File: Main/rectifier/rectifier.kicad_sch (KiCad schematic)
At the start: 15 parts, among them J2 Jack-DC, J3 Screw_Terminal_01x02, Q1 BS170, U1 ESP32-C3-WROOM-02, U2 LM2596S-5, U3 HC-SR04, U4 DM-OLED096-636

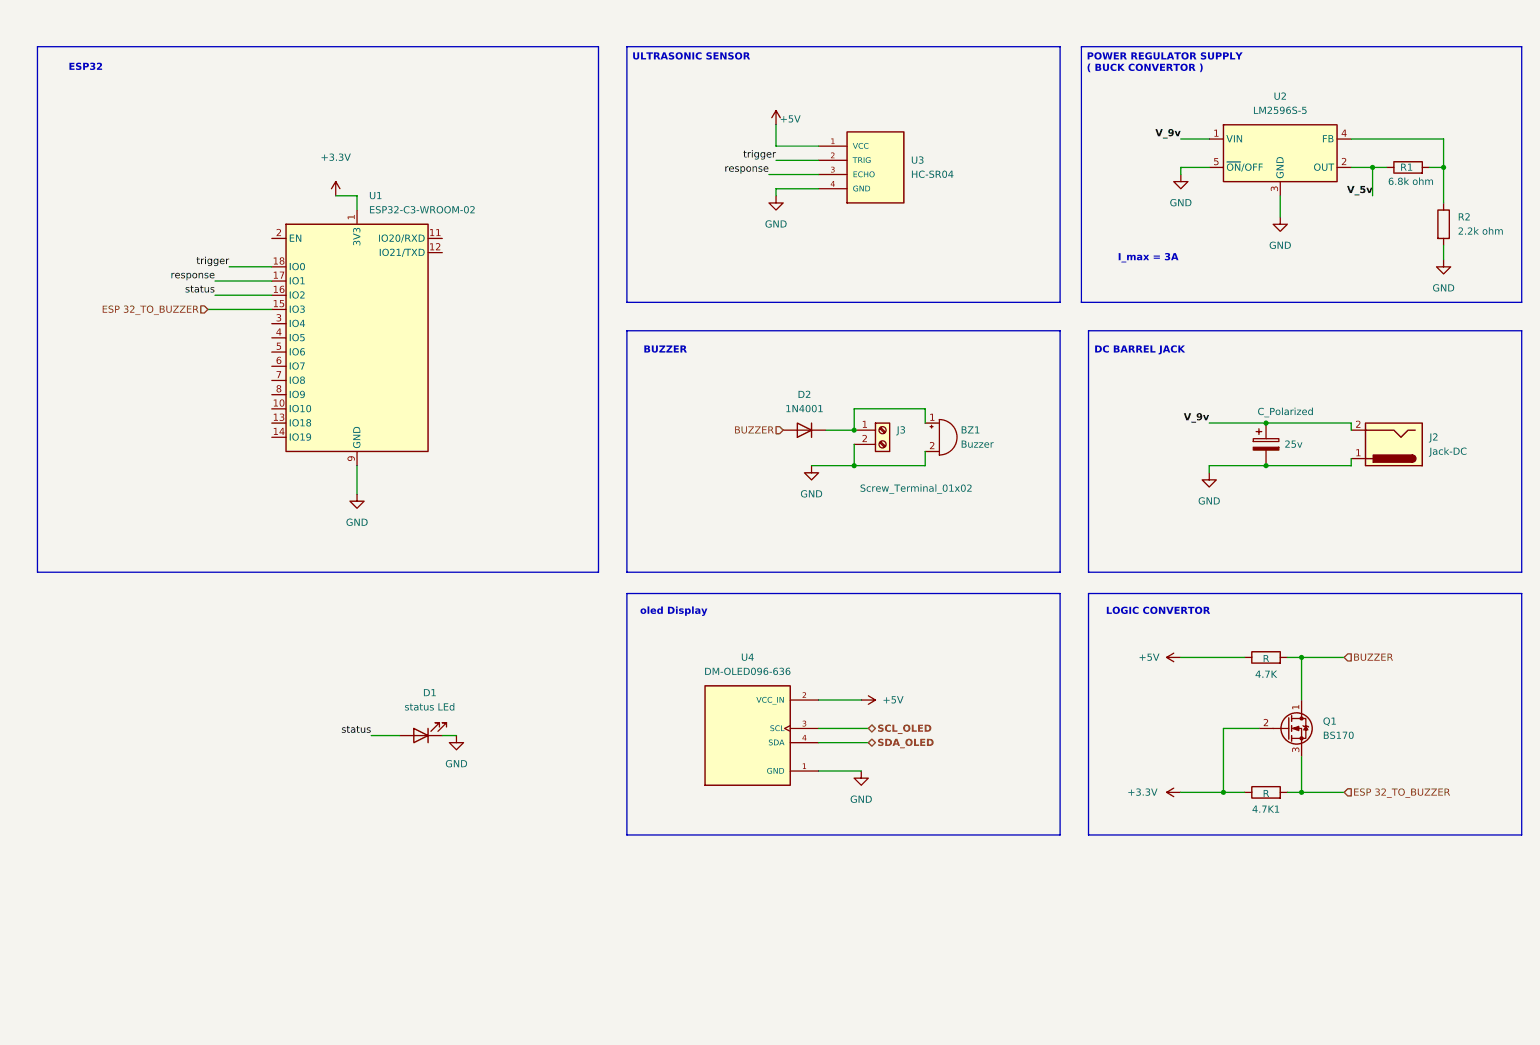
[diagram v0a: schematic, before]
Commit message: adding sim module to the schematic
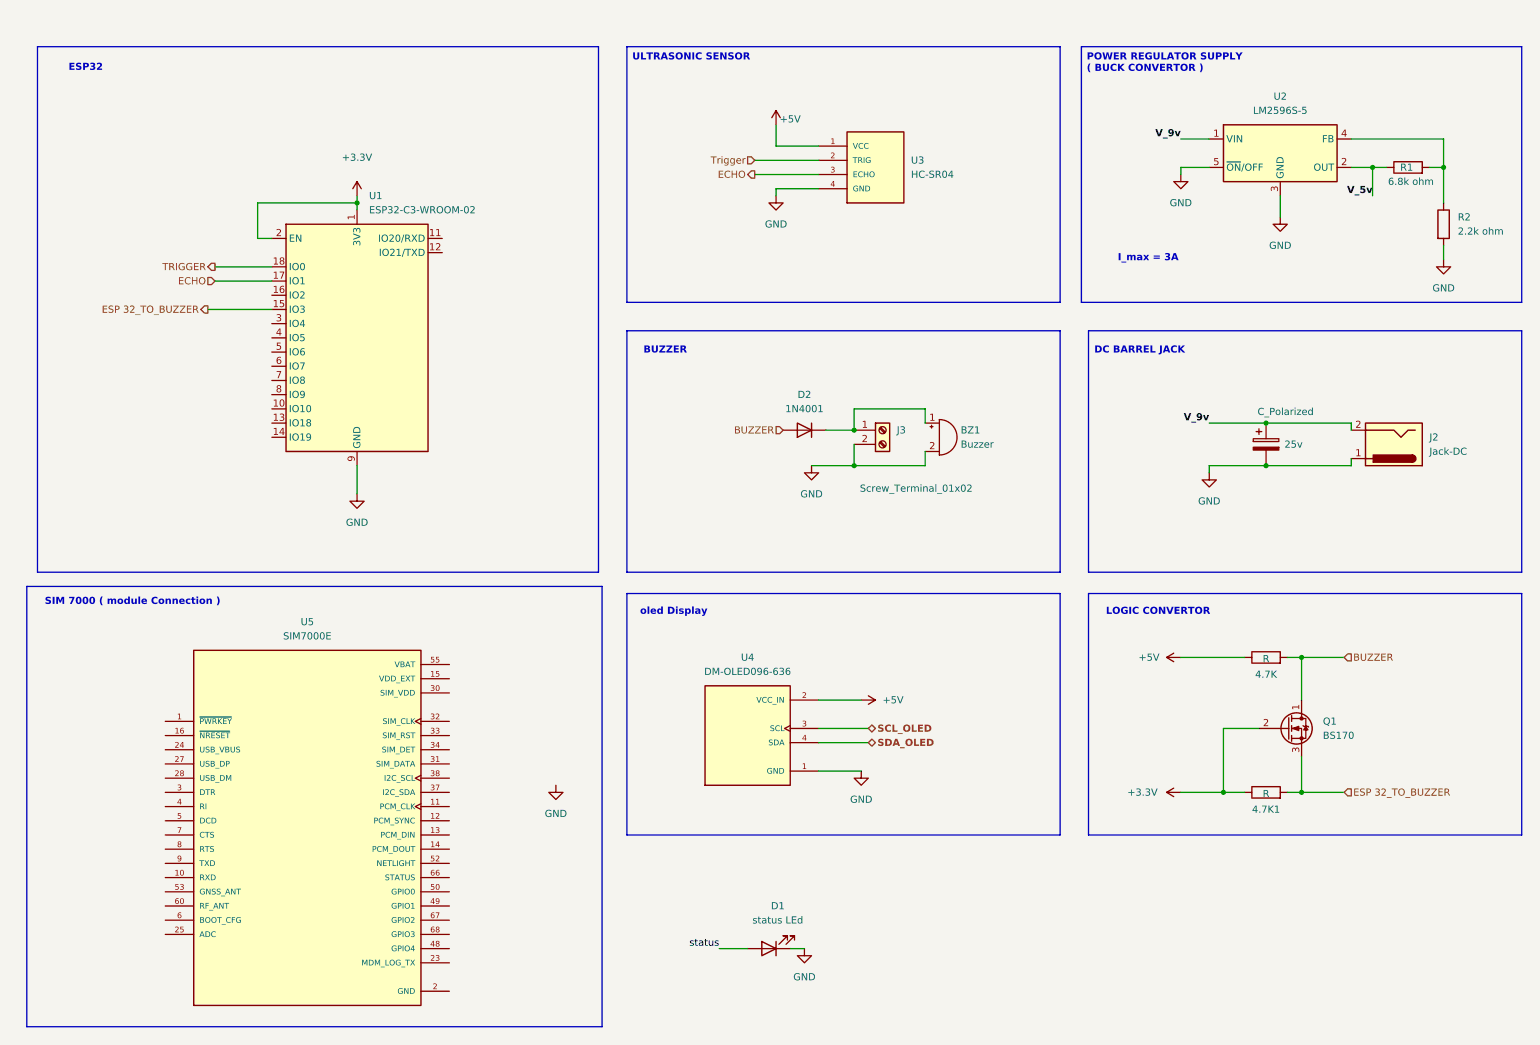
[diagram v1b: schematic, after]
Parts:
- added U5: SIM7000E, SIM7000E:SIMCON_SIM7000E, symbol SIM7000:SIM7000E
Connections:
- net +3.3V: now also U1.2 (EN)
- net GND: now also U5.17 (GND), U5.18 (GND), U5.2 (GND), U5.29 (GND), U5.39 (GND), U5.45 (GND), U5.46 (GND), U5.54 (GND), U5.58 (GND), U5.59 (GND), U5.61 (GND), U5.62 (GND), U5.63 (GND), U5.64 (GND), U5.65 (GND)
- net status: no longer U1.16 (IO2)
- net response renamed ECHO
- net trigger renamed TRIGGER
- net TRIGGER: no longer U3.2 (TRIG)
- new net Trigger: U3.2 (TRIG)
- new net VBAT: U5.55 (VBAT), U5.56 (VBAT), U5.57 (VBAT)
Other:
- note added: "SIM 7000 ( module Connection )"
- title: (none) -> CIRCUIT
- moved on the sheet: D1

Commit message: making connection for SIM modeule
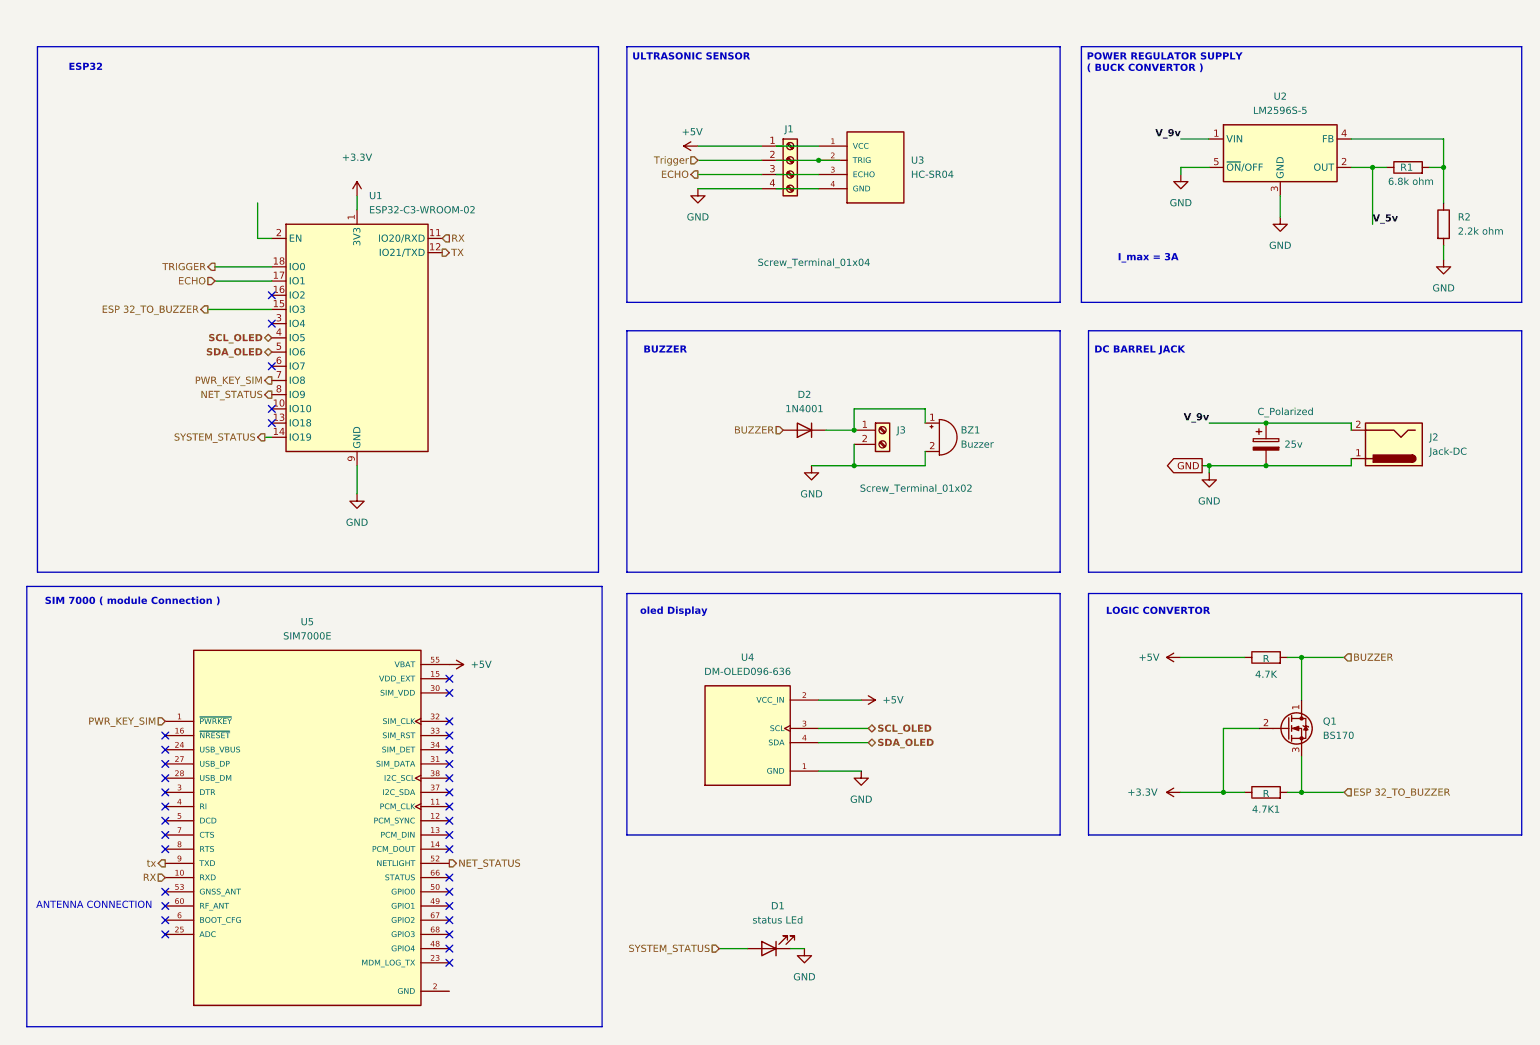
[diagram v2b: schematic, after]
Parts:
- added J1: Screw_Terminal_01x04, symbol Connector:Screw_Terminal_01x04
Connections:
- net VBAT is gone; now on net +5V: U5.55 (VBAT), U5.56 (VBAT), U5.57 (VBAT)
- net status is gone; now on net SYSTEM_STATUS: D1.2 (A)
- net +3.3V: no longer U1.2 (EN)
- net +5V: now also J1.1 (Pin_1); no longer U3.1 (VCC)
- net ECHO: now also J1.3 (Pin_3); no longer U3.3 (ECHO)
- net GND: now also J1.4 (Pin_4); no longer U3.4 (GND)
- net SCL_OLED: now also U1.4 (IO5)
- net SDA_OLED: now also U1.5 (IO6)
- net Trigger: now also J1.2 (Pin_2); no longer U3.2 (TRIG)
- net RX: now reaches U1.11 (IO20/RXD)
- net RX: now also U5.10 (RXD)
- net TX: now reaches U1.12 (IO21/TXD)
- net SYSTEM_STATUS: now reaches U1.14 (IO19)
- net PWR_KEY_SIM: now reaches U1.7 (IO8)
- net PWR_KEY_SIM: now also U5.1 (~{PWRKEY})
- net NET_STATUS: now reaches U1.8 (IO9)
- net NET_STATUS: now also U5.52 (NETLIGHT)
- net tx: now reaches U5.9 (TXD)
- no-connect marks 0 -> 37
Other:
- note added: "ANTENNA CONNECTION"

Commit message: updated schematic
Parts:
- removed D2: 1N4001, Diode_THT:D_DO-41_SOD81_P10.16mm_Horizontal, symbol Diode:1N4001
- removed J1: Screw_Terminal_01x04, symbol Connector:Screw_Terminal_01x04
- removed U2: LM2596S-5, Package_TO_SOT_SMD:TO-263-5_TabPin3, symbol Regulator_Switching:LM2596S-5
- added C1: 0.1uf, Capacitor_Tantalum_SMD:CP_EIA-1608-08_AVX-J_HandSolder, symbol Device:C_Polarized
- added C2: 100uf, Capacitor_Tantalum_SMD:CP_EIA-1608-08_AVX-J_HandSolder, symbol Device:C_Polarized
- added C3: C, Capacitor_SMD:C_0402_1005Metric_Pad0.74x0.62mm_HandSolder, symbol Device:C
- added J1: SIM_Card, Connector_JAE:JAE_SIM_Card_SF72S006, symbol Connector:SIM_Card
- added J3: U.FL-R-SMT_01_, U.FL-R-SMT_01_:HRS_U.FL-R-SMT_01_, symbol U.FL-R-SMT_01_:U.FL-R-SMT_01_
- added R3: R, Resistor_SMD:R_0402_1005Metric, symbol Device:R
- added S1: BUTT-2, BUTT-2:SW_BUTT-2, symbol PUSH_BUTT-2:BUTT-2
- BZ1: footprint (none) -> Buzzer_Beeper:Buzzer_TDK_PS1240P02BT_D12.2mm_H6.5mm
- C4: renamed from 25v; value C_Polarized -> 470uf
- J4: renamed from J2; footprint (none) -> Connector_BarrelJack:BarrelJack_GCT_DCJ200-10-A_Horizontal
- R1: value 6.8k ohm -> 10k ohm; footprint Resistor_THT:R_Box_L13.0mm_W4.0mm_P9.00mm -> Resistor_SMD:R_0402_1005Metric
- R2: value 2.2k ohm -> R; footprint Resistor_THT:R_Box_L13.0mm_W4.0mm_P9.00mm -> Resistor_SMD:R_0402_1005Metric
- renumbered 4.7K to 4.7K1, 4.7K1 to 4.7K2, J3 to J2, U5 to U1, U1 to U2, U4 to U3, U3 to U4
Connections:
- net V_5v is gone; now on net +3.3V: R1.1
- net tx is gone; now on net TX: U1.9 (TXD)
- net +3.3V: now also U2.2 (EN)
- net +5V: now also U4.1 (VCC), C1.1, C2.1
- net BUZZER: now also BZ1.1 (+), J2.1 (Pin_1)
- net ECHO: now also U4.3 (ECHO)
- net GND: now also U4.4 (GND), C1.2, C2.2, C3.2, J1.5 (GND), J3.1 (GND), J3.2 (GND), S1.1; no longer R2.2
- net PWR_KEY_SIM: now also R1.2, S1.2
- net TRIGGER: now also U4.2 (TRIG)
- net at R2.1: now also C3.1, R3.2; no longer R1.2
- net SIM_VDD: now reaches U1.30 (SIM_VDD)
- net SIM_VDD: now also J1.1 (VCC)
- net SIM_DATA : now reaches U1.31 (SIM_DATA)
- net SIM_DATA : now also J1.7 (I/O)
- net SIM Card CLK: now reaches U1.32 (SIM_CLK)
- net SIM Card CLK: now also J1.3 (CLK)
- net SIM Card RST: now reaches U1.33 (SIM_RST)
- net SIM Card RST: now also J1.2 (RST)
- net RF_ANTENNA: now reaches U1.60 (RF_ANT)
- net RF_ANTENNA: now also R2.2
- net SIM_MODULE_STATUS: now reaches U1.66 (STATUS)
- net SIM_MODULE_STATUS: now also D1.2 (A)
- net SYSTEM_STATUS: no longer names the net of U2.14 (IO19)
- net SYSTEM_STATUS: no longer D1.2 (A)
- net V_9v renamed +9V
- new net: J3.3 (SIG), R3.1
- no-connect marks 37 -> 33
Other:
- added sheet power management (untitled.kicad_sch)
- note added: "SIM_CARD_tray"
- note added: "SYSTEM STATUS"
- note removed: "I_max = 3A"
- moved on the sheet: 4.7K1, 4.7K2, BZ1, C4, D1, J2, J4, Q1, U1, U2, U3, U4
